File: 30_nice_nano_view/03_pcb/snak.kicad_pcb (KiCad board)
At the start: 2 copper layers, 114 x 100.2 mm, 164 parts

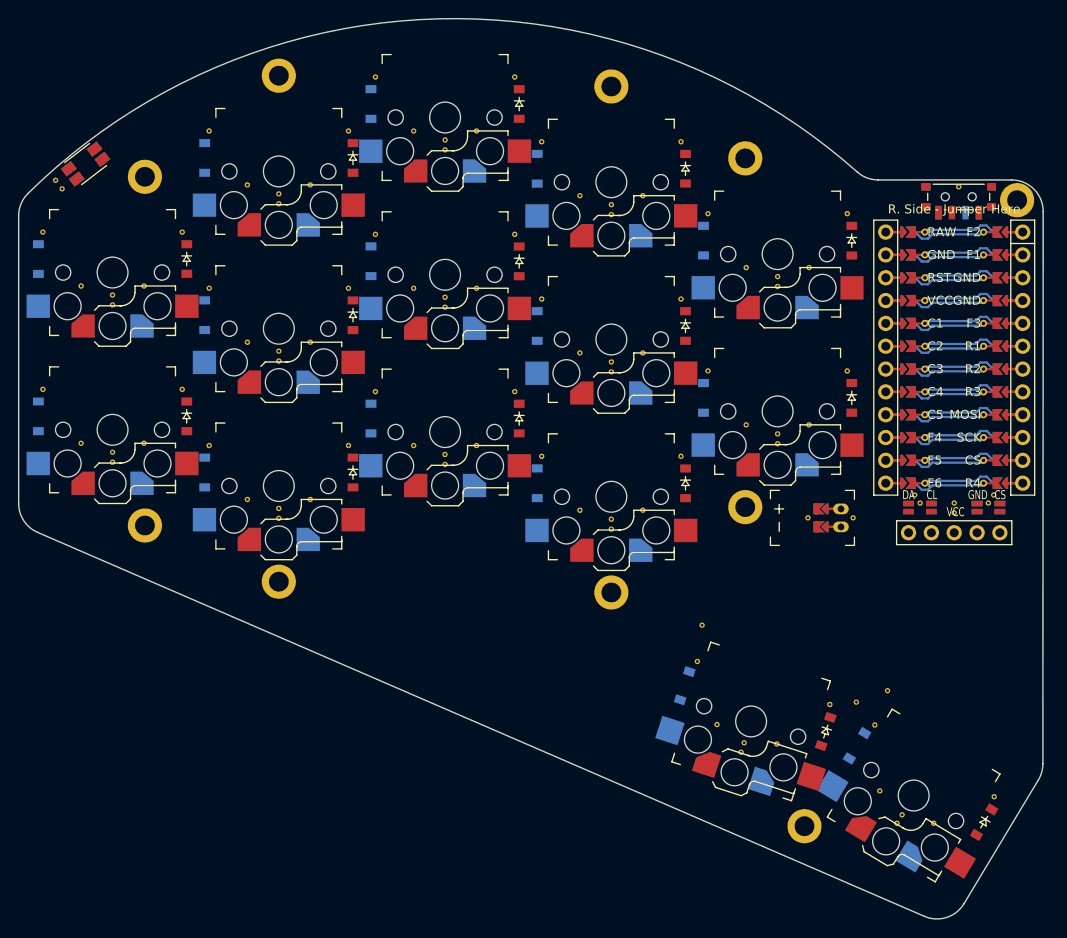
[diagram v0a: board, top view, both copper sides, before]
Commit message: update config and move reset and jst to on top of mcu
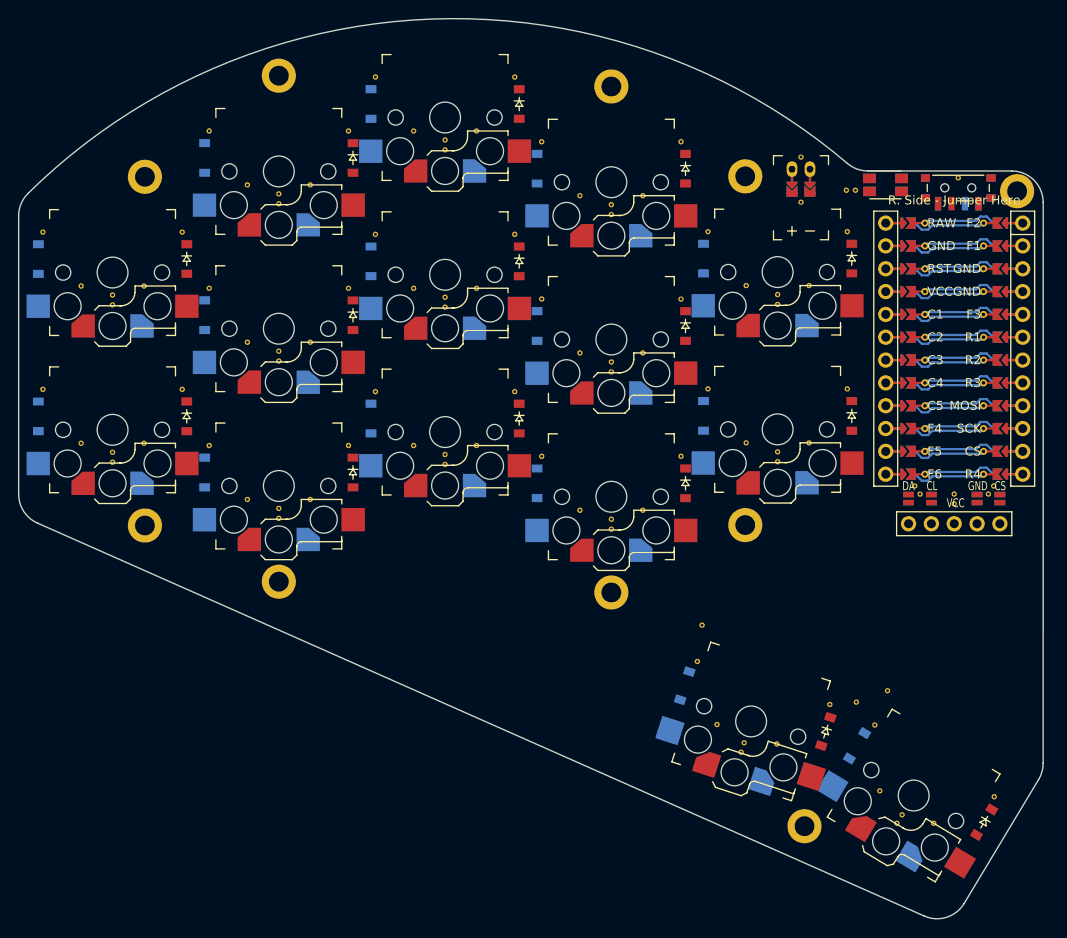
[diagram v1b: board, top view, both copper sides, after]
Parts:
- removed the REF** at (194.2, 55.5)
- removed the REF** at (177.4, 92.3)
- removed the REF** at (182.4, 92.3)
- removed the REF** at (93.7, 54.7)
- removed the REF** at (94.4, 55.7)
- removed the REF** at (181.8, 76.0)
- removed the REF** at (181.8, 58.5)
- removed the REF** at (177.5, 82.0)
- removed the REF** at (177.5, 64.5)
- removed the REF** at (166.2, 76.0)
- removed the REF** at (166.2, 58.5)
- removed the REF** at (170.5, 82.0)
- removed the REF** at (170.5, 64.5)
- removed the REF** at (174.0, 84.0)
- removed the REF** at (174.0, 66.5)
- removed the REF** at (174.0, 83.0)
- removed the REF** at (174.0, 65.5)
- removed the REF** at (189.2, 89.8)
- removed the REF** at (198.1, 89.8)
- removed the REF** at (193.7, 90.7)
- removed the REF** at (189.8, 90.7)
- removed the REF** at (197.5, 90.7)
- removed the REF** at (193.7, 91.8)
- added REF**: VIA-0.6mm, VIA-0.6mm, F.Cu at (194.1, 54.5)
- added REF**: VIA-0.6mm, VIA-0.6mm, F.Cu at (176.6, 57.2)
- added REF**: VIA-0.6mm, VIA-0.6mm, F.Cu at (176.6, 52.1)
- added REF**: VIA-0.6mm, VIA-0.6mm, F.Cu at (181.7, 55.8)
- added REF**: VIA-0.6mm, VIA-0.6mm, F.Cu at (182.7, 55.8)
- added REF**: VIA-0.6mm, VIA-0.6mm, F.Cu at (181.8, 78.0)
- added REF**: VIA-0.6mm, VIA-0.6mm, F.Cu at (181.8, 60.5)
- added REF**: VIA-0.6mm, VIA-0.6mm, F.Cu at (177.5, 84.0)
- added REF**: VIA-0.6mm, VIA-0.6mm, F.Cu at (177.5, 66.5)
- added REF**: VIA-0.6mm, VIA-0.6mm, F.Cu at (166.2, 78.0)
- added REF**: VIA-0.6mm, VIA-0.6mm, F.Cu at (166.2, 60.5)
- added REF**: VIA-0.6mm, VIA-0.6mm, F.Cu at (170.5, 84.0)
- added REF**: VIA-0.6mm, VIA-0.6mm, F.Cu at (170.5, 66.5)
- added REF**: VIA-0.6mm, VIA-0.6mm, F.Cu at (174.0, 86.0)
- added REF**: VIA-0.6mm, VIA-0.6mm, F.Cu at (174.0, 68.5)
- added REF**: VIA-0.6mm, VIA-0.6mm, F.Cu at (174.0, 85.0)
- added REF**: VIA-0.6mm, VIA-0.6mm, F.Cu at (174.0, 67.5)
- added REF**: VIA-0.6mm, VIA-0.6mm, F.Cu at (189.2, 88.8)
- added REF**: VIA-0.6mm, VIA-0.6mm, F.Cu at (198.1, 88.8)
- added REF**: VIA-0.6mm, VIA-0.6mm, F.Cu at (193.7, 89.7)
- added REF**: VIA-0.6mm, VIA-0.6mm, F.Cu at (189.8, 89.7)
- added REF**: VIA-0.6mm, VIA-0.6mm, F.Cu at (197.5, 89.7)
- added REF**: VIA-0.6mm, VIA-0.6mm, F.Cu at (193.7, 90.8)
- moved SW2 89.0 mm to (186.0, 55.2), turned to 90 degrees
- moved JST1 39.1 mm to (176.6, 53.5), turned to 0 degrees
- moved D12 2.00 mm to (182.2, 81.0)
- moved D13 2.00 mm to (182.2, 63.5)
- moved D27 2.00 mm to (165.8, 81.0)
- moved D28 2.00 mm to (165.8, 63.5)
- moved H7 2.00 mm to (170.4, 54.3)
- moved H8 2.00 mm to (170.4, 93.1)
- moved S12 2.00 mm to (174.0, 82.5)
- moved S13 2.00 mm to (174.0, 65.0)
- moved SW1 1.00 mm to (194.1, 55.6)
- moved DISP1 1.00 mm to (193.7, 76.2)
- moved H10 1.00 mm to (200.7, 56.0)
- moved MCU1 1.00 mm to (193.7, 72.2)
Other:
- outline, holes or cut-outs redrawn
